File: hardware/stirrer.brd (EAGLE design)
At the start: 71.1 x 66 mm, 53 parts, among them Q2 FDN306P, Q3 8 MHz, U1 PIC24FV16KM202, U2 A4960, U3 PIC24FV32KA302, X1 ICD, X2 Console

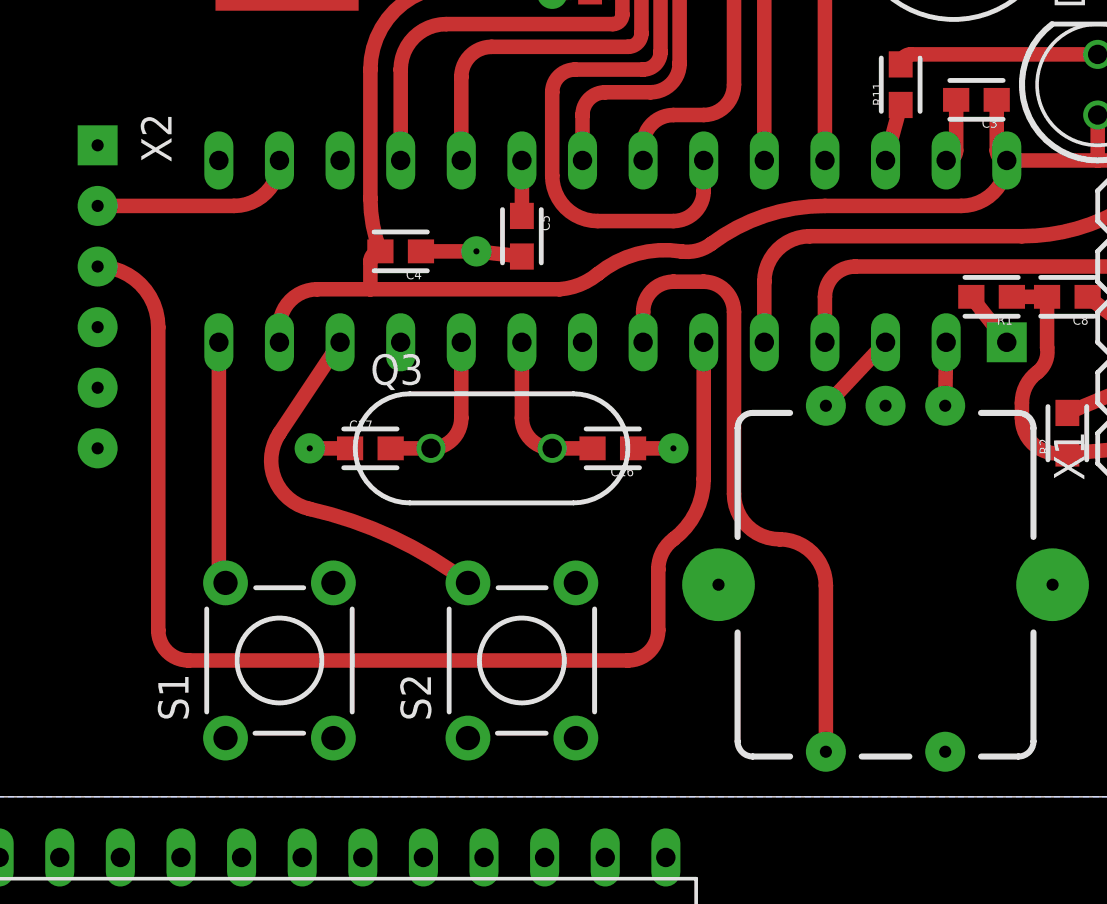
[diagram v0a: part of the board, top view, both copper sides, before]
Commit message: initial layout of display compartment
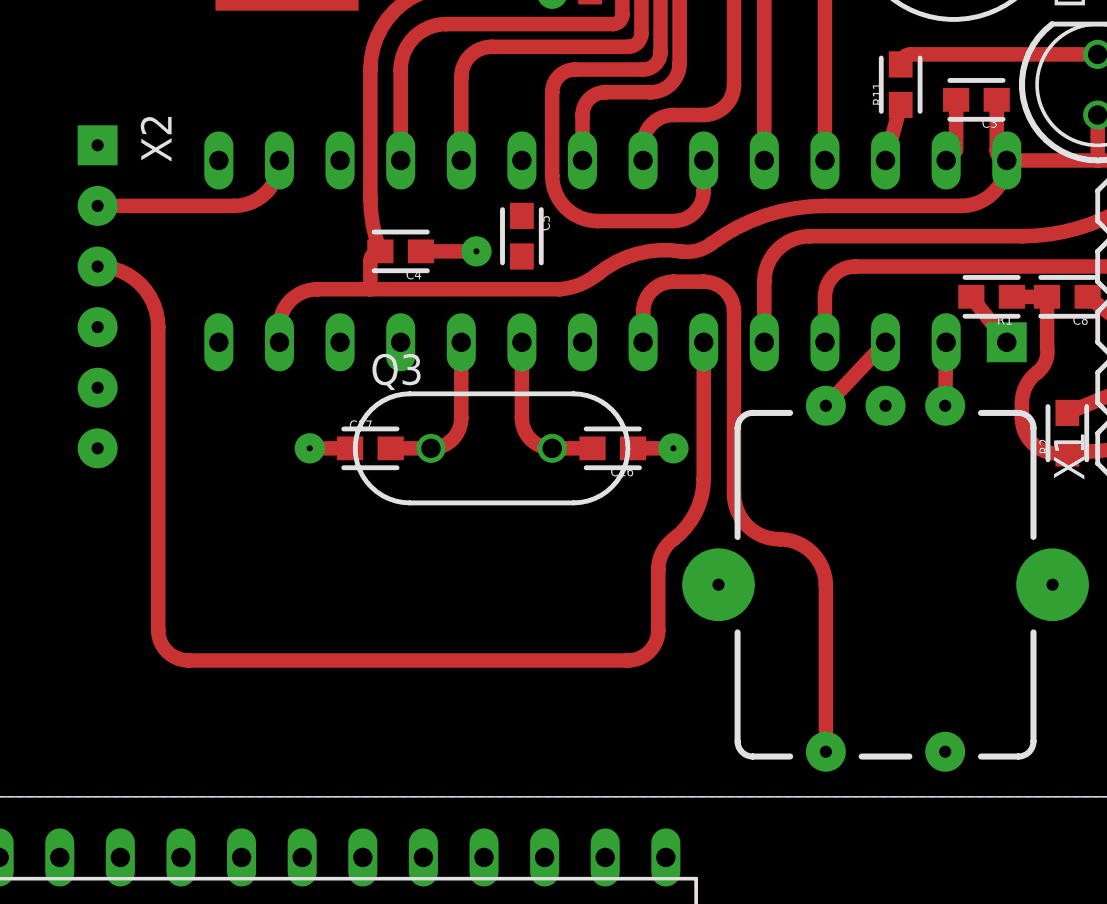
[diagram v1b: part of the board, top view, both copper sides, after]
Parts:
- removed S1: RUN, ch_passive:TACTILE-PTH
- removed S2: BRAKE, ch_passive:TACTILE-PTH
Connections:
- removed net BRAKE_SW: S2.1, S2.2, U1.12
- removed net RUN_SW: S1.1, S1.2, U1.14
- net GND: now also U3.27, U3.8; no longer S1.3, S1.4, S2.3, S2.4, U1.27, U1.8
- net N$1: now also U3.20; no longer U1.20
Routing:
- net BRAKE_SW: track 15.3 -> 0.00 mm
- net RUN_SW: track 10.2 -> 0.00 mm
- net GND: track 33.0 -> 30.5 mm
- net N$1: track 2.33 -> 0.00 mm
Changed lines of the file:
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@@
 <element name="R8" library="ch_passive" package="0603" value="10" x="36.5125" y="49.8475" rot="R90"/>
 <element name="R9" library="ch_passive" package="0603" value="10" x="38.4175" y="50.165" rot="R90"/>
-<element name="S1" library="ch_passive" package="TACTILE-PTH" value="RUN" x="20.6375" y="5.715" rot="R90"/>
-<element name="S2" library="ch_passive" package="TACTILE-PTH" value="BRAKE" x="30.7975" y="5.715" rot="R90"/>
 <element name="U1" library="ch_microchip" package="DIL28-3" value="PIC24FV16KM202" x="34.6075" y="22.86" rot="MR0"/>
 <element name="U2" library="ch_allegro" package="LQPF-32" value="A4960" x="34.6075" y="41.91"/>
@@
 <contactref element="C1" pad="N"/>
 <contactref element="C2" pad="2"/>
-<contactref element="C5" pad="2"/>
-<contactref element="U1" pad="27"/>
-<contactref element="U1" pad="8"/>
 <contactref element="C3" pad="2"/>
 <contactref element="C4" pad="1"/>
 <contactref element="X2" pad="6"/>
-<contactref element="S1" pad="3"/>
-<contactref element="S2" pad="3"/>
-<contactref element="S2" pad="4"/>
-<contactref element="S1" pad="4"/>
 <contactref element="C10" pad="1"/>
 <contactref element="C11" pad="1"/>
@@
 </polygon>
 <wire x1="48.9975" y1="29.21" x2="48.9975" y2="27.09" width="0.6096" layer="1"/>
-<wire x1="48.9975" y1="27.09" x2="48.5775" y2="26.67" width="0.6096" layer="1" curve="-90"/>
 <via x="21.9075" y="14.605" extent="1-16" drill="0.254" diameter="1.27"/>
 <via x="28.8925" y="22.86" extent="1-16" drill="0.254" diameter="1.27"/>
 <via x="32.0675" y="33.655" extent="1-16" drill="0.254" diameter="1.27"/>
-<wire x1="28.8925" y1="22.86" x2="30.7975" y2="22.645" width="0.6096" layer="1"/>
 <wire x1="33.655" y1="33.7575" x2="32.0675" y2="33.655" width="0.6096" layer="1"/>
 <wire x1="26.5675" y1="22.86" x2="28.8925" y2="22.86" width="0.6096" layer="1"/>
@@
 <wire x1="33.4075" y1="40.71" x2="34.6075" y2="41.91" width="0.4064" layer="1" curve="90"/>
 <wire x1="54.61" y1="38.6325" x2="57.785" y2="39.37" width="1.016" layer="1"/>
+<contactref element="C5" pad="2"/>
+<contactref element="U3" pad="8"/>
+<contactref element="U3" pad="27"/>
+<wire x1="57.785" y1="39.37" x2="67.31" y2="59.69" width="0" layer="19" extent="1-1"/>
+<wire x1="47.02" y1="36.83" x2="54.61" y2="38.6325" width="0" layer="19" extent="1-1"/>
+<wire x1="48.9975" y1="29.21" x2="47.02" y2="36.83" width="0" layer="19" extent="1-1"/>
+<wire x1="54.5075" y1="20.955" x2="48.9975" y2="27.09" width="0" layer="19" extent="1-1"/>
+<wire x1="46.0375" y1="16.39" x2="54.5075" y2="20.955" width="0" layer="19" extent="1-1"/>
+<wire x1="37.1475" y1="14.605" x2="46.0375" y2="16.39" width="0" layer="19" extent="1-1"/>
+<wire x1="30.7975" y1="22.645" x2="35.4575" y2="14.605" width="0" layer="19" extent="1-1"/>
+<wire x1="28.8925" y1="22.86" x2="30.7975" y2="22.645" width="0" layer="19" extent="1-1"/>
+<wire x1="23.5975" y1="14.605" x2="26.5675" y2="22.86" width="0" layer="19" extent="1-1"/>
+<wire x1="13.0175" y1="14.605" x2="21.9075" y2="14.605" width="0" layer="19" extent="1-1"/>
+<wire x1="32.0675" y1="33.655" x2="30.7975" y2="22.645" width="0" layer="19" extent="1-1"/>
+<wire x1="30.2575" y1="39.91" x2="32.0675" y2="33.655" width="0" layer="19" extent="1-1"/>
+<wire x1="25.615" y1="45.4025" x2="25.7175" y2="39.875" width="0" layer="19" extent="1-1"/>
+<wire x1="48.5375" y1="1.89" x2="46.0375" y2="16.39" width="0" layer="19" extent="1-1"/>
+<wire x1="6.35" y1="-2.54" x2="13.0175" y2="14.605" width="0" layer="19" extent="1-1"/>
+<wire x1="21.59" y1="-10.16" x2="6.35" y2="-2.54" width="0" layer="19" extent="1-1"/>
 </signal>
 <signal name="+5V">
@@
 <wire x1="35.8775" y1="27.305" x2="35.8775" y2="26.67" width="0.6096" layer="1"/>
 </signal>
-<signal name="N$1">
-<contactref element="U1" pad="20"/>
-<contactref element="C5" pad="1"/>
-<wire x1="30.7975" y1="26.67" x2="30.7975" y2="24.345" width="0.6096" layer="1"/>
-</signal>
 <signal name="PWM">
 <contactref element="U2" pad="6"/>
@@
 <wire x1="49.6325" y1="20.955" x2="51.1175" y2="19.05" width="0.6096" layer="1"/>
 </signal>
-<signal name="RUN_SW">
-<contactref element="S1" pad="1"/>
-<contactref element="S1" pad="2"/>
-<contactref element="U1" pad="14"/>
-<wire x1="18.0975" y1="19.05" x2="18.0975" y2="9.2456" width="0.6096" layer="1"/>
-<wire x1="18.0975" y1="9.2456" x2="18.3769" y2="8.9662" width="0.6096" layer="1" curve="90"/>
-<wire x1="18.3769" y1="2.4638" x2="18.3769" y2="8.9662" width="0" layer="19" extent="1-1"/>
-</signal>
-<signal name="BRAKE_SW">
-<contactref element="S2" pad="1"/>
-<contactref element="S2" pad="2"/>
-<contactref element="U1" pad="12"/>
-<wire x1="23.1775" y1="19.05" x2="20.6375" y2="15.24" width="0.6096" layer="1"/>
-<wire x1="20.6375" y1="15.24" x2="21.9075" y2="12.065" width="0.6096" layer="1" curve="110.982954"/>
-<wire x1="21.9075" y1="12.065" x2="28.5369" y2="8.9662" width="0.6096" layer="1" curve="-24.691648"/>
-<wire x1="28.5369" y1="2.4638" x2="28.5369" y2="8.9662" width="0" layer="19" extent="1-1"/>
-</signal>
 <signal name="N$9">
 <contactref element="R11" pad="2"/>
@@
 <wire x1="43.4975" y1="20.955" x2="43.4975" y2="19.05" width="0.6096" layer="1"/>
 </signal>
+<signal name="N$1">
+<contactref element="U3" pad="20"/>
+<contactref element="C5" pad="1"/>
+<wire x1="24.13" y1="-2.54" x2="30.7975" y2="24.345" width="0" layer="19" extent="1-1"/>
+</signal>
 </signals>
